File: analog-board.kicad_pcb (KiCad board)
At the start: 2 copper layers, 200 x 150 mm, 488 parts, among them J1 AC IN, J2 OUT, J3 CONN_20X2, P2 CONN_01X02, Q1 2N3906, Q10 2N3906, Q11 2N3906, Q12 2N3906, Q13 2N3906, Q14 2N3906, Q15 2N3906, Q16 2N3906, Q17 NPN, Q18 NPN, Q19 J111, Q2 2N3906, Q20 2N3906, Q3 2N3906, Q4 2N3906, Q5 2N3906, Q6 BCM857BS, Q7 2N3906, Q8 2N3906, Q9 2N3906, U1 LM13700, U10 ADR01, U11 DG212B, U12 DG212B, U13 DG408, U14 DG408, U15 TL072-, U16 DG408, U17 DG408, U18 LM13700, U19 LM13700, U2 LM13700, U21 TL072-, U22 TL074-, U23 TL074-, U24 TL074-, U25 TL074-, U26 TL072-, U27 TL074-, U28 TL074-, U29 LM13700, U3 LM13700, U30 LM13700, U31 TL074-, U32 LM13700, U33 TL074-, U34 TL074-, U35 TL074-, U36 74LV573, U38 0 - 10V, U39 TL074-, U4 DG212B, U40 DG419, U41 0 - 10V, U42 10 - 0V, U43 LM7812, U44 LM7912, U45 DG408, U46 7805, U5 TL074-, U6 AD5556, U7 TL072-, U8 TL074-, U9 AD8672

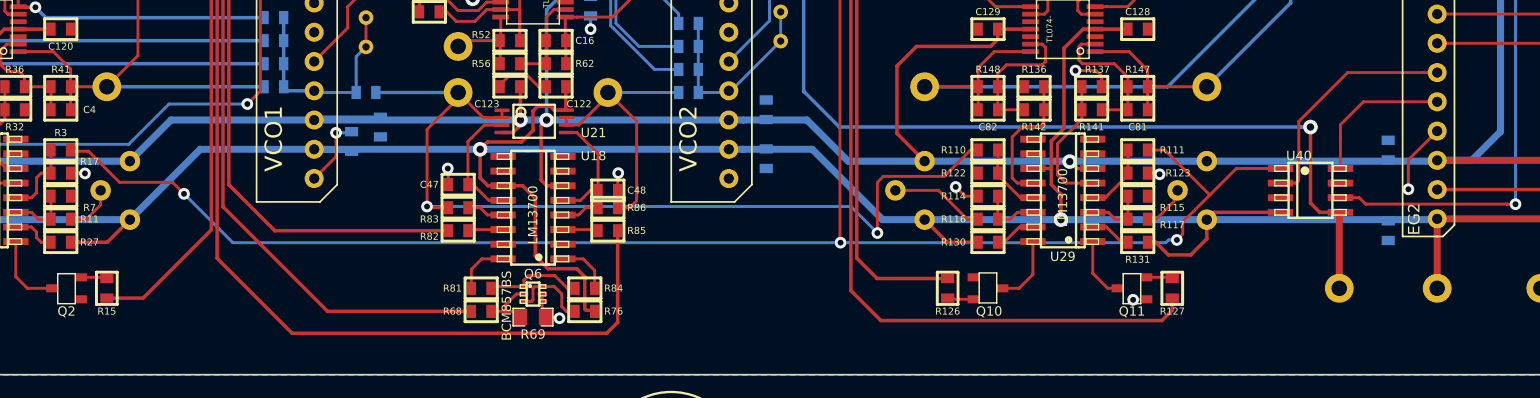
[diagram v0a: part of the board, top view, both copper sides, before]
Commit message: CV and GATE test points added and routed
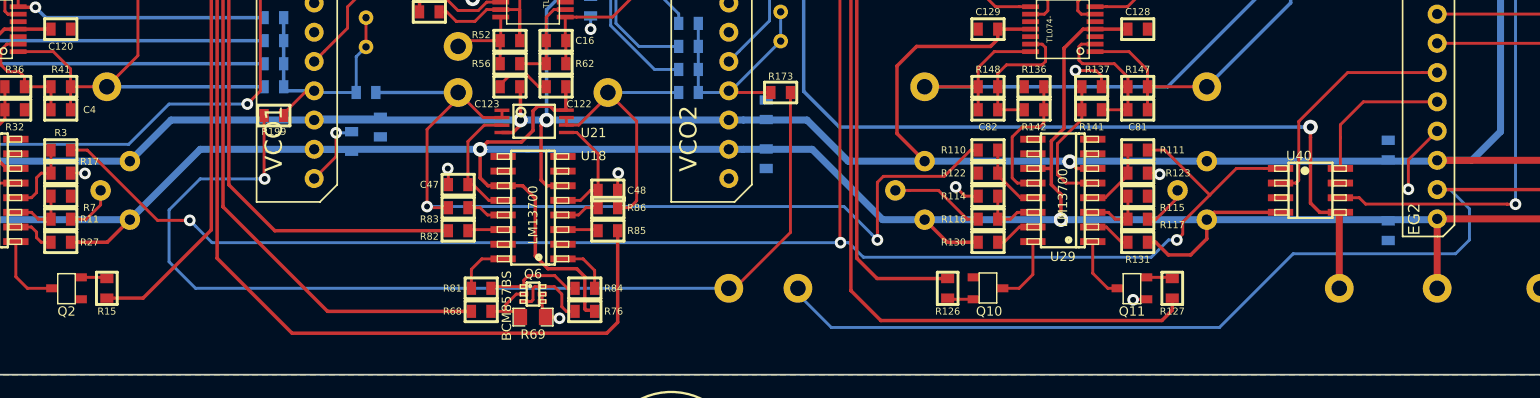
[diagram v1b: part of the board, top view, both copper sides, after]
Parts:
- added R173: 100K, MyModules:SM0603-R-JRL, F.Cu at (94.5, 125.5)
- added R199: 100K, MyModules:SM0603-R-JRL, F.Cu at (50.5, 127.5)
- added TP38: CONN_1, MyModules:TEST POINT, B.Cu at (90.0, 142.5)
- added TP39: CONN_1, MyModules:TEST POINT, B.Cu at (96.0, 142.5)
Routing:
- net EXT_CV_IN: track 0.00 -> 88.5 mm, vias 0 -> 1
- net GATE: track 159.8 -> 229.1 mm
- net Net-(R173-Pad1): track 17.5 -> 21.2 mm
- net Net-(R199-Pad1): track 19.4 -> 23.0 mm
- net EG2: track 261.0 -> 262.0 mm
- net OSCA GLIDE CV: track 79.8 -> 80.6 mm

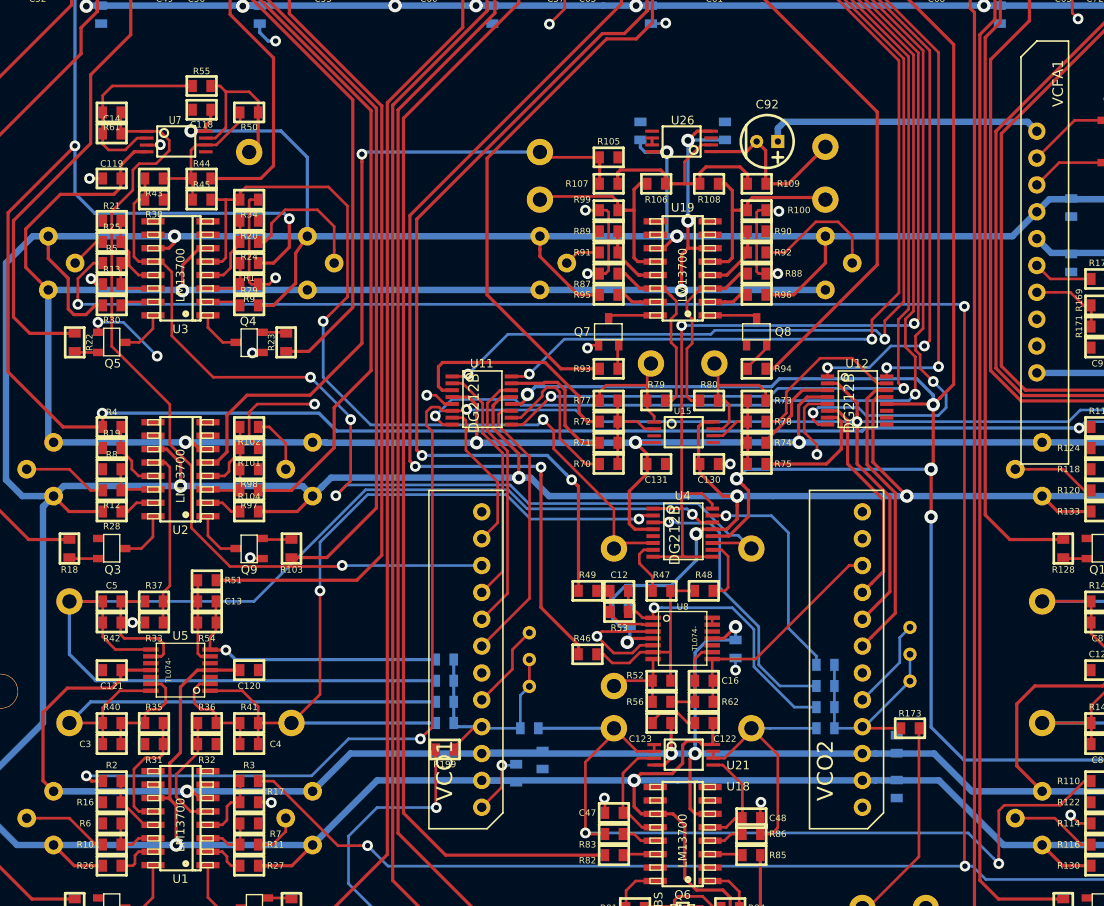
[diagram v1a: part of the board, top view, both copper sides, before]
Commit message: adjusted EXT CV input to VCO1, more silkscreen work
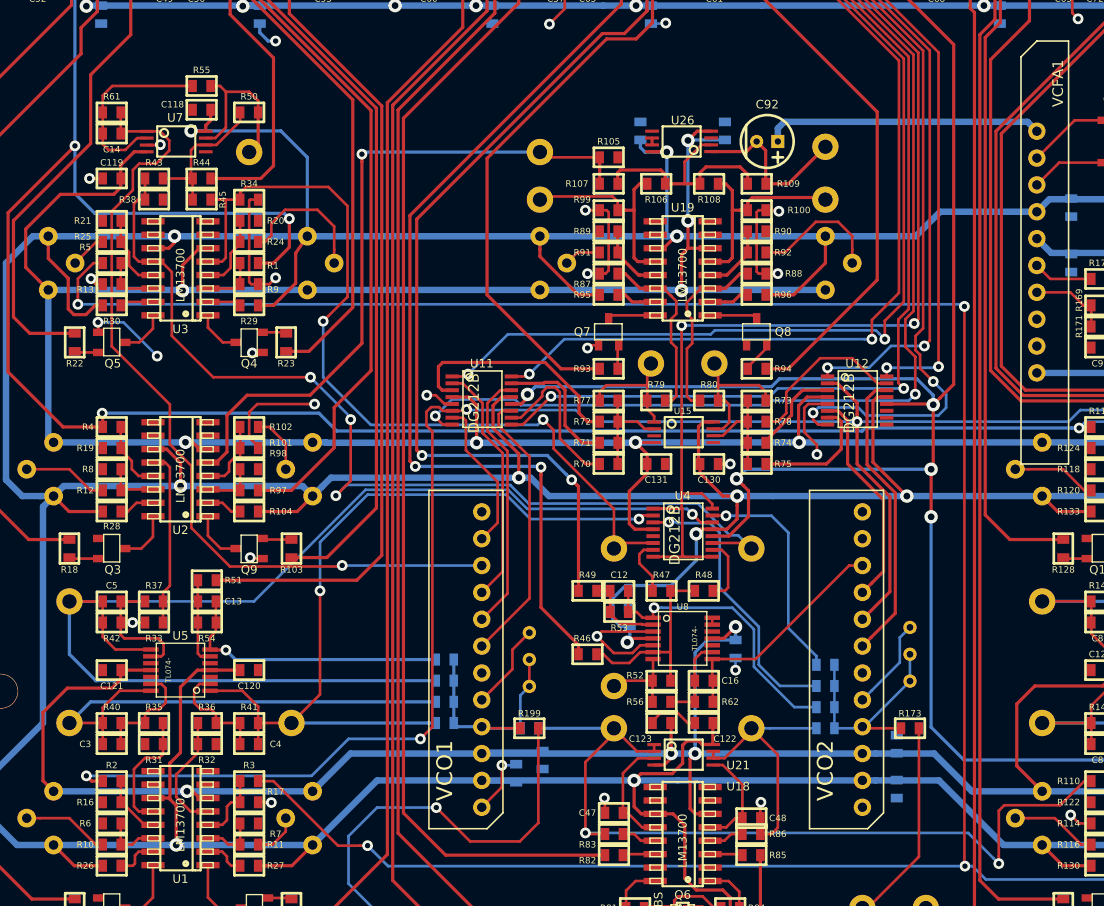
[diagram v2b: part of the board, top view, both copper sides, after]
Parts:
- moved R199 8.25 mm to (58.5, 125.5), turned to 0 degrees
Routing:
- net EXT_CV_IN: track 88.5 -> 103.7 mm
- net OSCB MIX CV: track 53.0 -> 53.8 mm

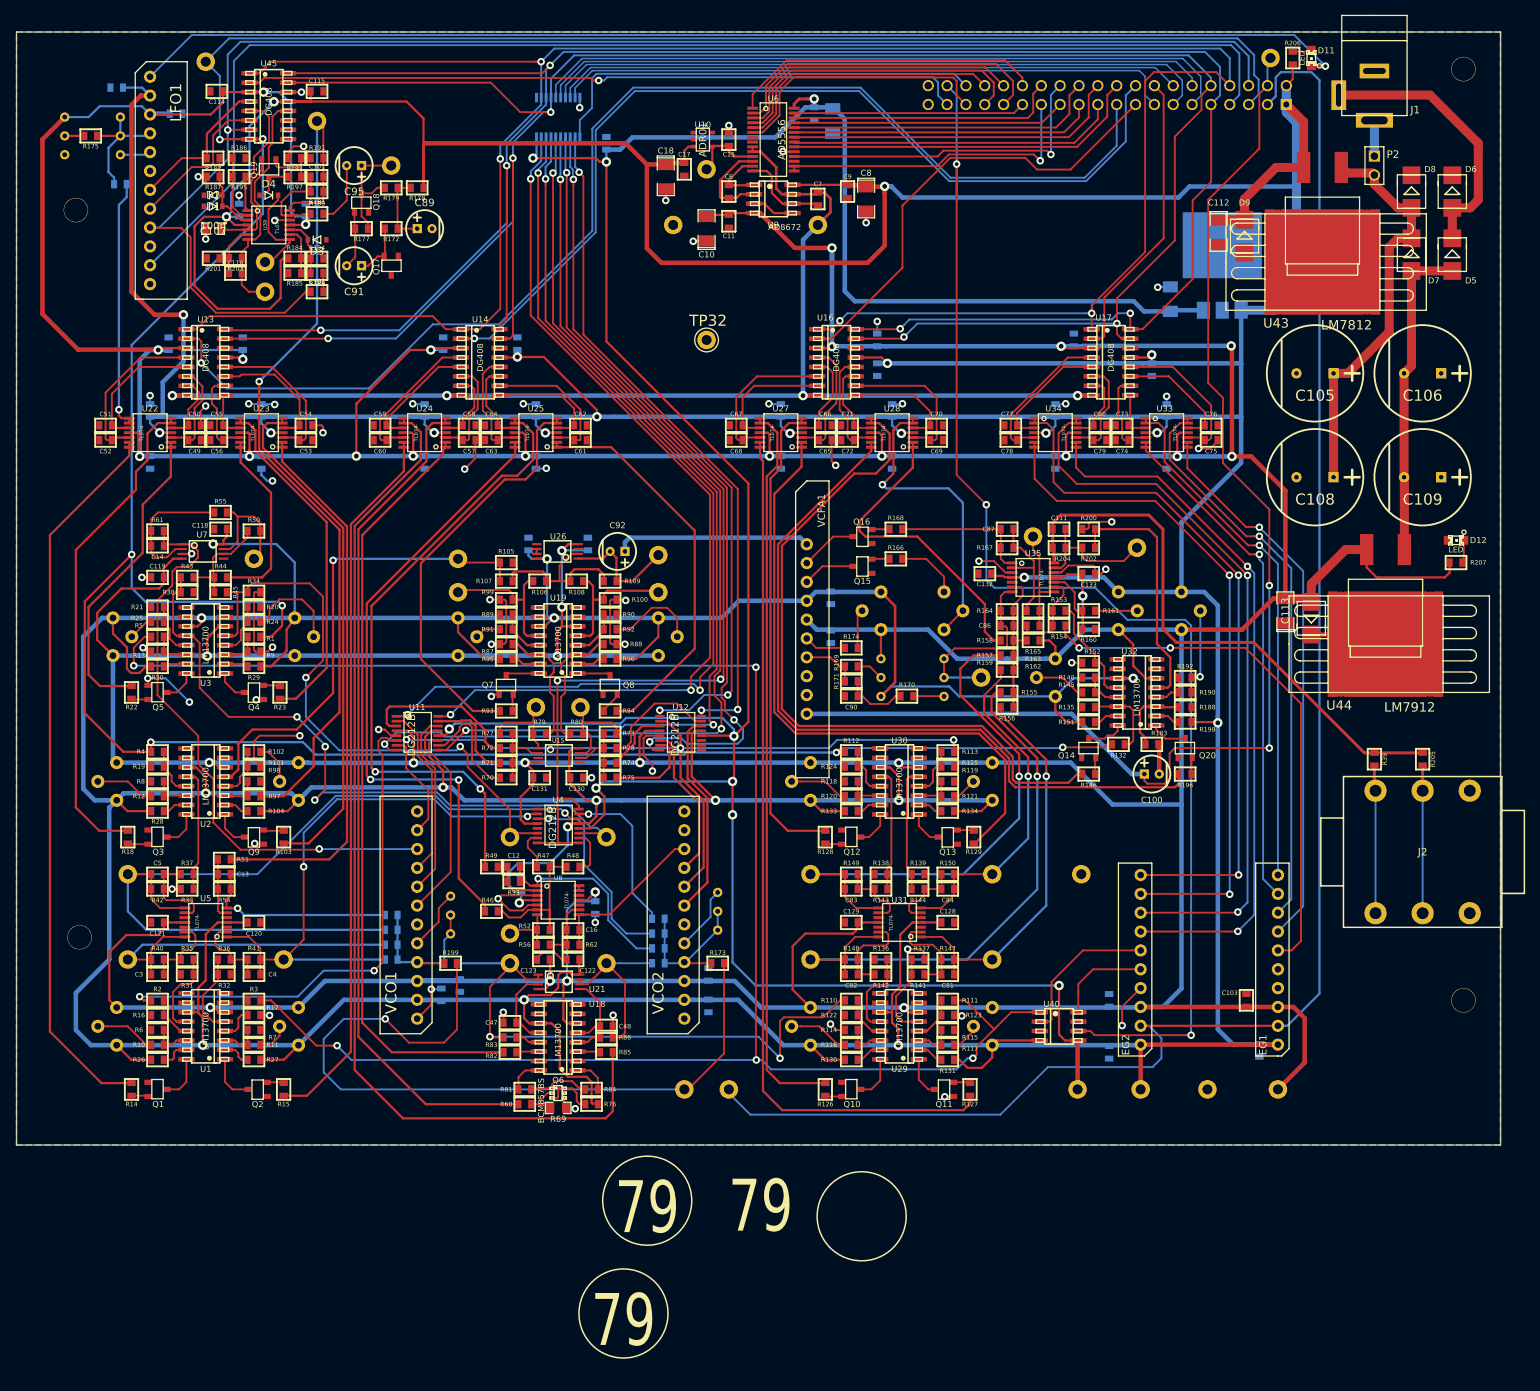
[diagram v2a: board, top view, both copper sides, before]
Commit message: silkscreen top layer mostly done, need to do bottom layer next
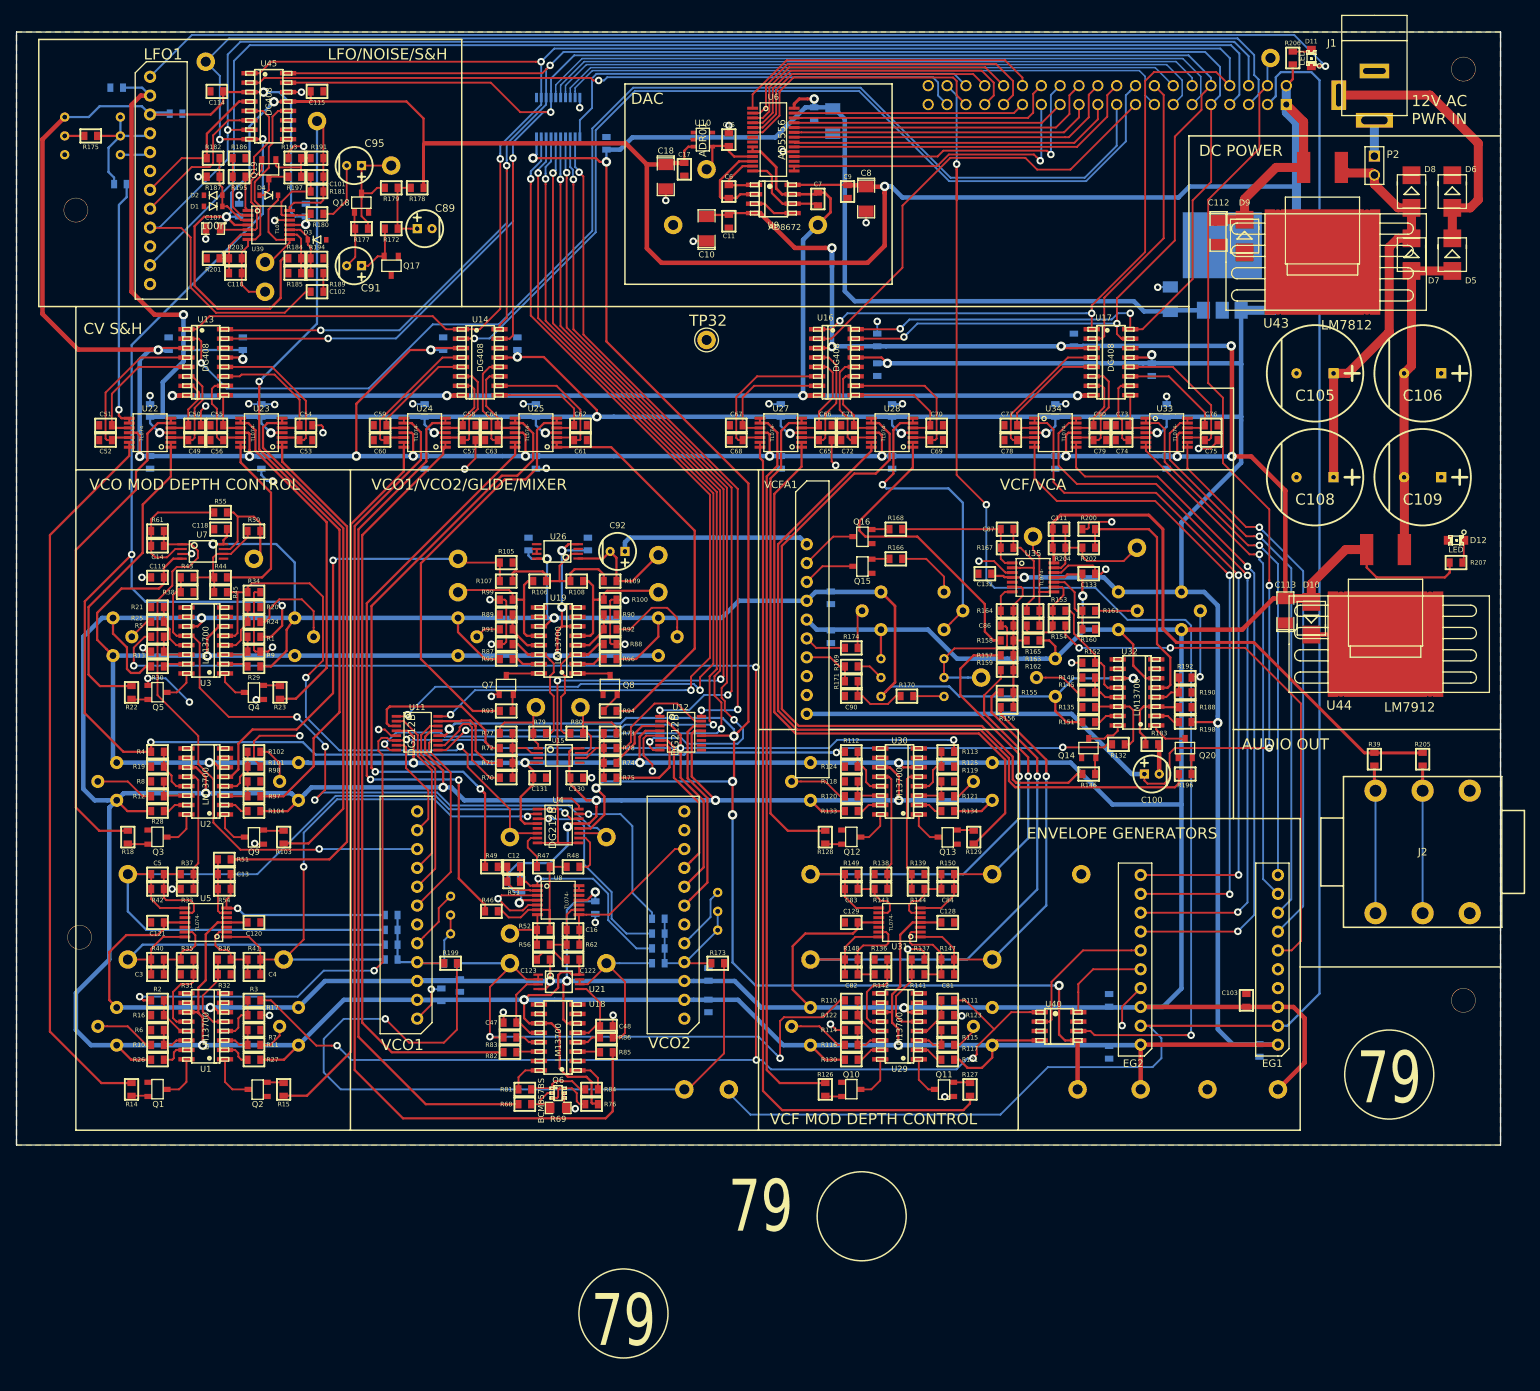
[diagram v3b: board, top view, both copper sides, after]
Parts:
- moved U41 101.4 mm to (185.0, 140.5)
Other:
- board text added: "12V AC PWR IN"
- board text added: "AUDIO OUT"
- board text added: "CV S&H"
- board text added: "DAC"
- board text added: "DC POWER"
- board text added: "ENVELOPE GENERATORS"
- board text added: "LFO/NOISE/S&H"
- board text added: "VCF MOD DEPTH CONTROL"
- board text added: "VCF/VCA"
- board text added: "VCO MOD DEPTH CONTROL"
- board text added: "VCO1/VCO2/GLIDE/MIXER"

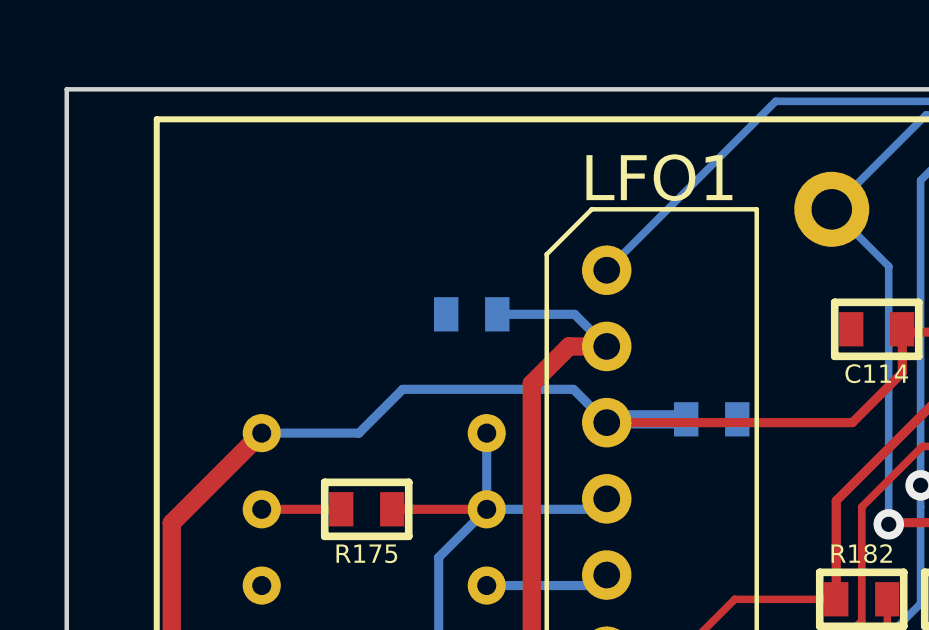
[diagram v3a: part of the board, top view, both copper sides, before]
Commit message: started silkscreen polishing on bottom layer
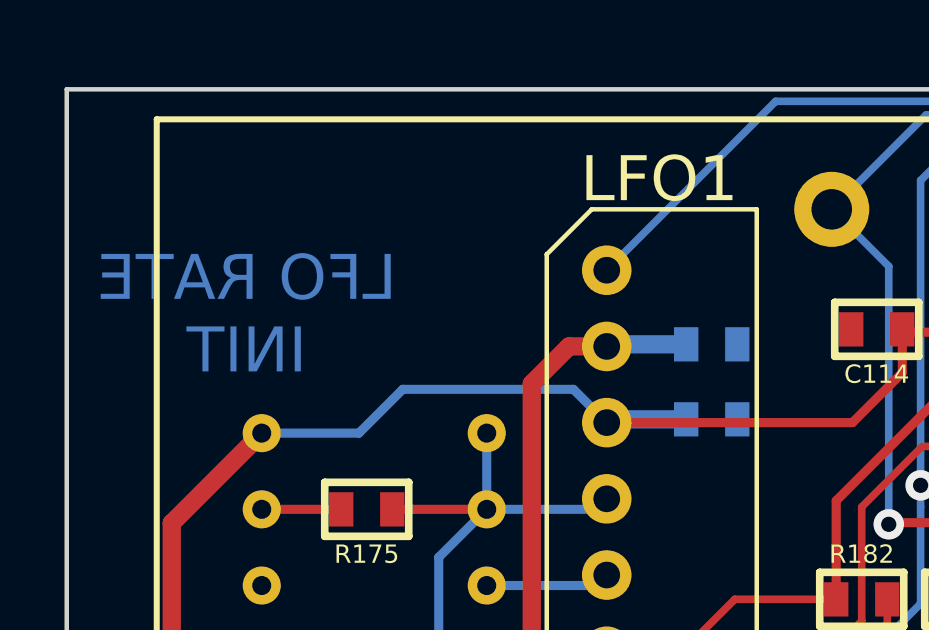
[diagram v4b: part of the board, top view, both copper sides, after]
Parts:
- moved C98 8.06 mm to (21.5, 8.50), turned to 0 degrees
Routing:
- net +12V: track 1642.6 -> 1641.1 mm
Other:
- board text added: "LFO OUT"
- board text added: "LFO RATE CV SCALE"
- board text added: "LFO RATE INIT"
- board text added: "NOISE"

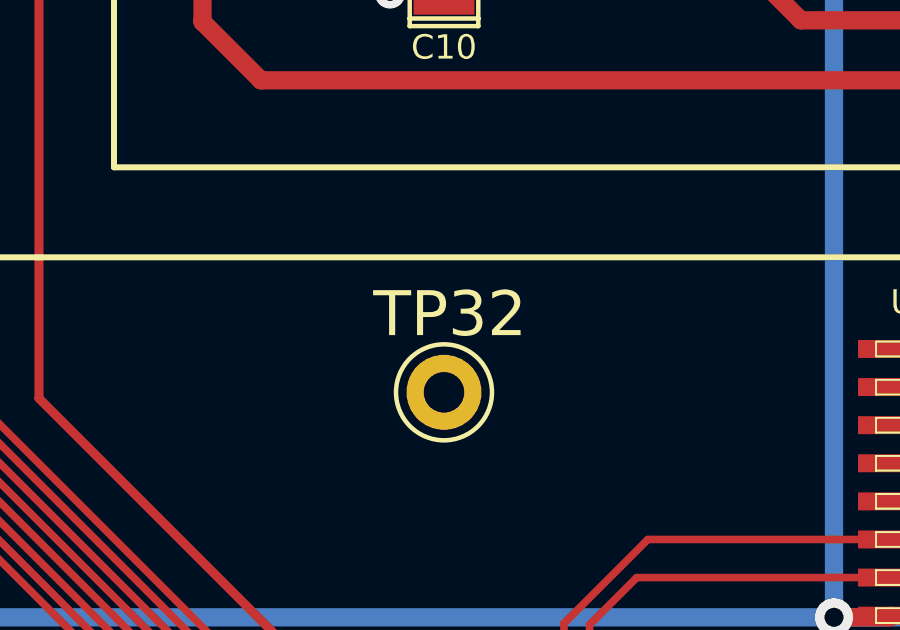
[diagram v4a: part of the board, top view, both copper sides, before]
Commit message: bottom layer silkscreen work
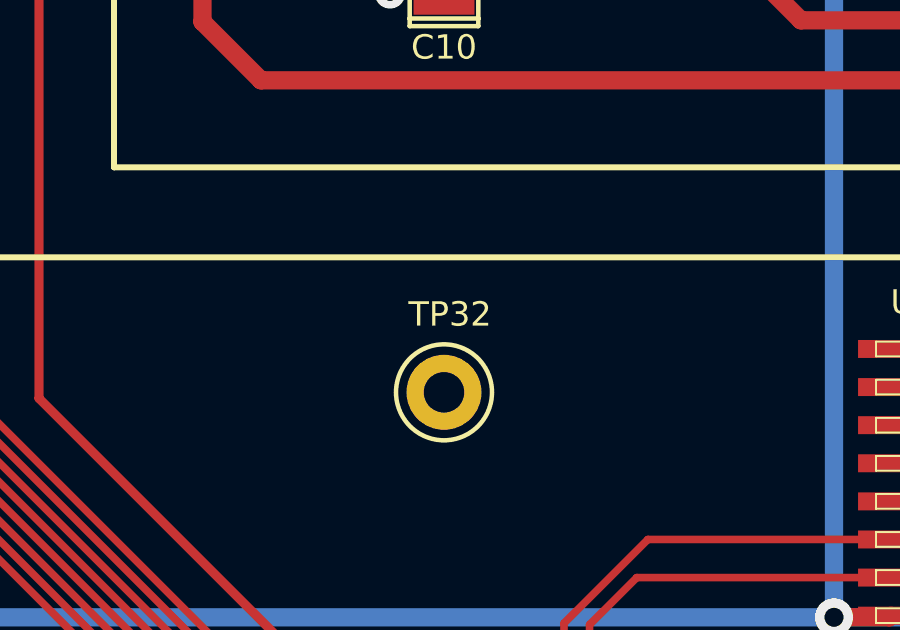
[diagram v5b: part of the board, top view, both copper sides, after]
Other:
- board text added: "TUNE"
